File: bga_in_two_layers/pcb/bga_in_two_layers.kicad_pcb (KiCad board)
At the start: 2 copper layers, 25.4 x 35.6 mm, 31 parts, among them CON1 top, CON2 left, CON3 right, CON4 bottom

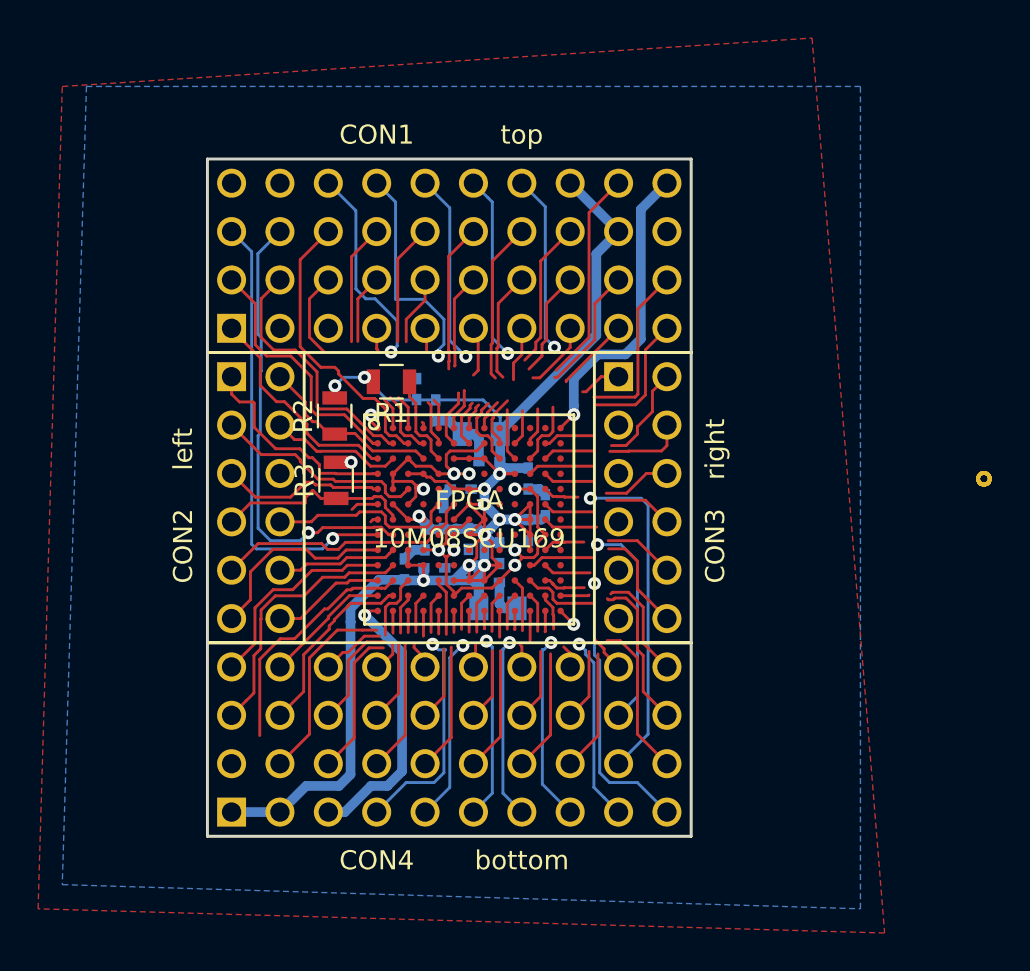
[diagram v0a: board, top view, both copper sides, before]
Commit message: bga_in_two_layers: finished routing, and sent off to oshpark
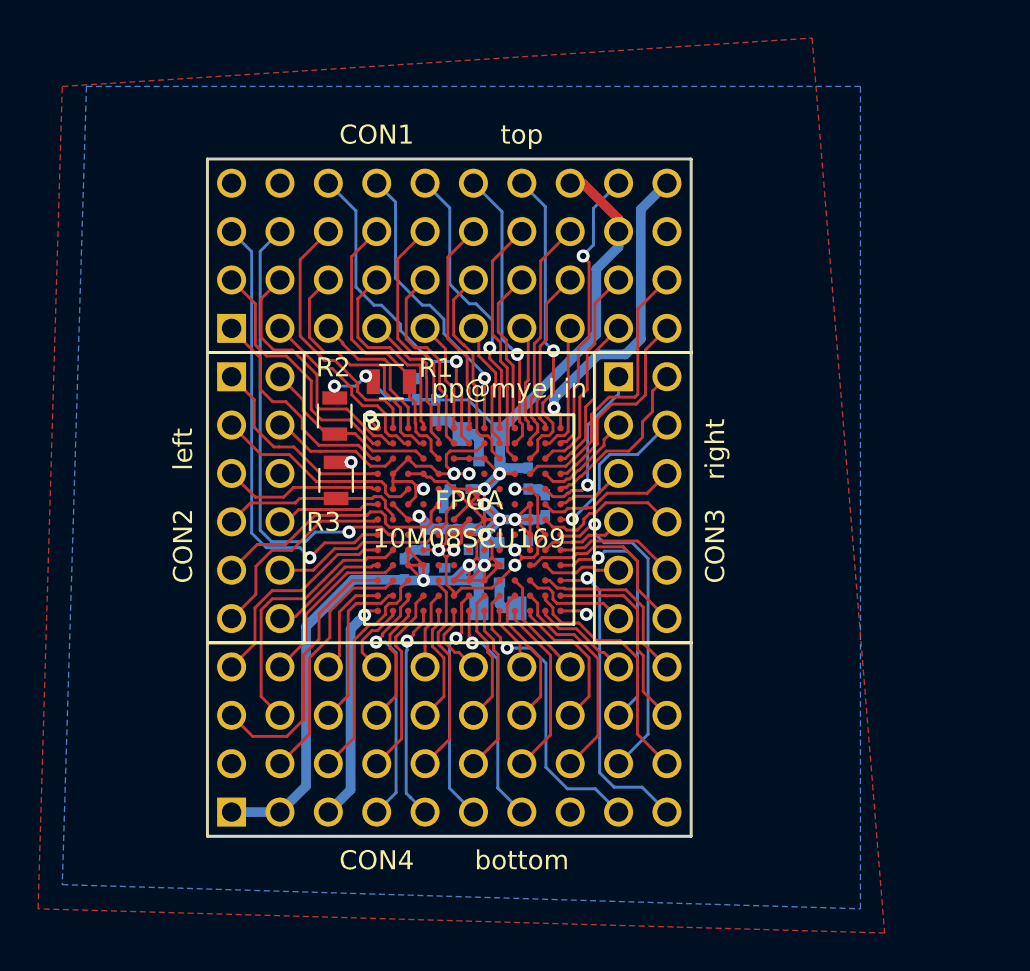
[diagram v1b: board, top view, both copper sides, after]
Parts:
- removed staple_single1, staple_single2, staple_single3, staple_single4, staple_single5, staple_single6, staple_single7: , myelin-kicad:via_single
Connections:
- CON1 pad 10: pin10 -> IO47
- CON1 pad 11: IO46 -> IO0
- CON1 pad 12: pin12 -> IO50
- CON1 pad 13: pin13 -> IO48
- CON1 pad 14: pin14 -> IO2
- CON1 pad 15: pin15 -> fpga_CONF_DONE
- CON1 pad 16: pin16 -> IO6
- CON1 pad 17: pin17 -> IO4
- CON1 pad 18: pin18 -> IO49
- CON1 pad 19: pin19 -> IO3
- CON1 pad 20: pin20 -> IO7
- CON1 pad 21: pin21 -> fpga_DEV_CLRn
- CON1 pad 22: pin22 -> IO70
- CON1 pad 23: pin23 -> IO5
- CON1 pad 24: pin24 -> IO51
- CON1 pad 25: pin25 -> IO9
- CON1 pad 26: pin26 -> IO8
- CON1 pad 27: pin27 -> IO71
- CON1 pad 28: pin28 -> IO85
- CON1 pad 29: pin29 -> IO72
- CON1 pad 30: pin30 -> IO10
- CON1 pad 31: pin31 -> IO52
- CON1 pad 33: pin33 -> IO34
- CON1 pad 34: pin34 -> IO73
- CON1 pad 36: pin36 -> IO33
- CON1 pad 37: pin37 -> IO35
- CON1 pad 38: pin38 -> IO74
- CON1 pad 5: pin5 -> IO46
- CON1 pad 9: pin9 -> IO1
- CON2 pad 10: IO66 -> fpga_TDO
- CON2 pad 11: IO28 -> fpga_TMS
- CON2 pad 12: VREFB2N0 -> IO30
- CON2 pad 8: fpga_TDI -> IO26
- CON2 pad 9: fpga_TDO -> fpga_TDI
- CON3 pad 1: pin1 -> IO76
- CON3 pad 10: pin10 -> IO40
- CON3 pad 11: pin11 -> IO82
- CON3 pad 12: pin12 -> IO80
- CON3 pad 2: pin2 -> CLK3n
- CON3 pad 3: pin3 -> IO75
- CON3 pad 4: pin4 -> IO38
- CON3 pad 5: pin5 -> CLK3p
- CON3 pad 6: pin6 -> IO77
- CON3 pad 7: pin7 -> IO79
- CON3 pad 8: pin8 -> IO78
- CON3 pad 9: pin9 -> IO81
- CON4 pad 10: pin10 -> IO69
- CON4 pad 11: pin11 -> IO53
- CON4 pad 12: pin12 -> IO32
- CON4 pad 13: pin13 -> IO54
- CON4 pad 14: pin14 -> IO55
- CON4 pad 15: pin15 -> DPCLK1
- CON4 pad 16: pin16 -> DPCLK0
- CON4 pad 17: pin17 -> IO13
- CON4 pad 18: pin18 -> IO87
- CON4 pad 19: pin19 -> IO14
- CON4 pad 20: pin20 -> IO56
- CON4 pad 21: pin21 -> IO57
- CON4 pad 22: pin22 -> IO17
- CON4 pad 23: pin23 -> IO58
- CON4 pad 24: pin24 -> IO15
- CON4 pad 25: pin25 -> IO16
- CON4 pad 26: pin26 -> IO19
- CON4 pad 27: pin27 -> IO60
- CON4 pad 28: pin28 -> IO18
- CON4 pad 3: IO67 -> VREFB2N0
- CON4 pad 30: pin30 -> IO61
- CON4 pad 31: pin31 -> IO20
- CON4 pad 32: pin32 -> IO84
- CON4 pad 33: pin33 -> IO59
- CON4 pad 34: pin34 -> IO39
- CON4 pad 35: pin35 -> IO42
- CON4 pad 36: pin36 -> IO21
- CON4 pad 37: pin37 -> IO43
- CON4 pad 38: pin38 -> IO62
- CON4 pad 39: pin39 -> IO44
- CON4 pad 4: IO30 -> IO28
- CON4 pad 40: pin40 -> IO83
- CON4 pad 6: IO69 -> IO68
- CON4 pad 7: IO53 -> IO66
- CON4 pad 8: IO32 -> IO67
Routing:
- net pin34: track 24.0 -> 0.00 mm, vias 1 -> 0
- net pin37: track 21.3 -> 0.00 mm, vias 1 -> 0
- net 3V3: track 110.3 -> 131.1 mm
- net pin12: track 19.6 -> 0.00 mm, vias 1 -> 0
- net IO39: track 0.00 -> 17.3 mm, vias 0 -> 1
- net pin38: track 17.2 -> 0.00 mm
- net IO43: track 0.00 -> 16.3 mm, vias 0 -> 1
- net pin10: track 16.0 -> 0.00 mm
- net IO33: track 0.00 -> 15.3 mm, vias 0 -> 1
- net IO50: track 2.51 -> 17.7 mm, vias 0 -> 1
- net IO7: track 0.00 -> 14.9 mm, vias 0 -> 1
- net IO59: track 2.04 -> 16.0 mm, vias 0 -> 1
- net IO6: track 1.63 -> 15.4 mm, vias 0 -> 1
- net pin33: track 13.6 -> 0.00 mm, vias 1 -> 0
- net pin16: track 13.2 -> 0.00 mm, vias 1 -> 0
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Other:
- board text added: "myelin.nz/ acorn/bgain2"
- board text added: "pp@myel.in"

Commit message: Renumbered IO* pins to match connector pinout
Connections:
- net CLK3n renamed C3_2_CLK3n
- net CLK3p renamed C3_3_CLK3p
- net DPCLK0 renamed C4_16_DPCLK0
- net DPCLK1 renamed C4_15_DPCLK1
- net IO0 renamed C1_11
- net IO1 renamed C1_9
- net IO10 renamed C1_30
- net IO13 renamed C4_17
- net IO14 renamed C4_19
- net IO15 renamed C4_24
- net IO16 renamed C4_25
- net IO17 renamed C4_22
- net IO18 renamed C4_28
- net IO19 renamed C4_26
- net IO2 renamed C1_14
- net IO20 renamed C4_31
- net IO21 renamed C4_36
- net IO22 renamed C1_2
- net IO23 renamed C1_1
- net IO24 renamed C2_1
- net IO25 renamed C2_5
- net IO26 renamed C2_8
- net IO27 renamed C1_3
- net IO28 renamed C4_4
- net IO3 renamed C1_19
- net IO30 renamed C2_12
- net IO32 renamed C4_12
- net IO33 renamed C1_36
- net IO34 renamed C1_33
- net IO35 renamed C1_37
- net IO38 renamed C3_4
- net IO39 renamed C4_34
- net IO4 renamed C1_17
- net IO40 renamed C3_10
- net IO42 renamed C4_35
- net IO43 renamed C4_37
- net IO44 renamed C4_39
- net IO45 renamed C1_6
- net IO46 renamed C1_5
- net IO47 renamed C1_10
- net IO48 renamed C1_13
- net IO49 renamed C1_18
- net IO5 renamed C1_23
- net IO50 renamed C1_12
- net IO51 renamed C1_24
- net IO52 renamed C1_31
- net IO53 renamed C4_11
- net IO54 renamed C4_13
- net IO55 renamed C4_14
- net IO56 renamed C4_20
- net IO57 renamed C4_21
- net IO58 renamed C4_23
- net IO59 renamed C4_33
- net IO6 renamed C1_16
- net IO60 renamed C4_27
- net IO61 renamed C4_30
- net IO62 renamed C4_38
- net IO63 renamed C2_4
- net IO65 renamed C1_7
- net IO66 renamed C4_7
- net IO67 renamed C4_8
- net IO68 renamed C4_6
- net IO69 renamed C4_10
- net IO7 renamed C1_20
- net IO70 renamed C1_22
- net IO71 renamed C1_27
- net IO72 renamed C1_29
- net IO73 renamed C1_34
- net IO74 renamed C1_38
- net IO75 renamed C3_3
- net IO76 renamed C3_1
- net IO77 renamed C3_6
- net IO78 renamed C3_8
- net IO79 renamed C3_7
- net IO8 renamed C1_26
- net IO80 renamed C3_12
- net IO81 renamed C3_9
- net IO82 renamed C3_11
- net IO83 renamed C4_40
- net IO84 renamed C4_32
- net IO85 renamed C1_28
- net IO86 renamed C2_3
- net IO87 renamed C4_18
- net IO9 renamed C1_25
- net VREFB2N0 renamed C4_3_VREFB2N0

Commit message: bga_in_two_layers bringup
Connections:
- net C3_3_CLK3p renamed C3_5_CLK3p
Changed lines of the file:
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@@
   (net 99 C1_9)
   (net 100 C3_2_CLK3n)
-  (net 101 C3_3_CLK3p)
-  (net 102 C4_3_VREFB2N0)
-  (net 103 C4_15_DPCLK1)
-  (net 104 C4_16_DPCLK0)
+  (net 101 C4_3_VREFB2N0)
+  (net 102 C4_15_DPCLK1)
+  (net 103 C4_16_DPCLK0)
+  (net 104 C3_5_CLK3p)
   (net_class Default "This is the default net class."
     (clearance 0.1524)
@@
     (add_net C3_2_CLK3n)
     (add_net C3_3)
-    (add_net C3_3_CLK3p)
     (add_net C3_4)
+    (add_net C3_5_CLK3p)
     (add_net C3_6)
     (add_net C3_7)
@@
       (net 60 C3_6))
     (pad F13 smd circle (at 4.8 -0.8) (size 0.342 0.342) (layers F.Cu F.Paste F.Mask)
-      (net 101 C3_3_CLK3p))
+      (net 104 C3_5_CLK3p))
     (pad G1 smd circle (at -4.8 0) (size 0.342 0.342) (layers F.Cu F.Paste F.Mask)
       (net 9 fpga_TMS))
@@
       (net 93 C4_35))
     (pad L1 smd circle (at -4.8 3.2) (size 0.342 0.342) (layers F.Cu F.Paste F.Mask)
-      (net 102 C4_3_VREFB2N0))
+      (net 101 C4_3_VREFB2N0))
     (pad L2 smd circle (at -4 3.2) (size 0.342 0.342) (layers F.Cu F.Paste F.Mask)
       (net 68 C4_6))
@@
       (net 1 GND))
     (pad N2 smd circle (at -4 4.8) (size 0.342 0.342) (layers F.Cu F.Paste F.Mask)
-      (net 104 C4_16_DPCLK0))
+      (net 103 C4_16_DPCLK0))
     (pad N3 smd circle (at -3.2 4.8) (size 0.342 0.342) (layers F.Cu F.Paste F.Mask)
-      (net 103 C4_15_DPCLK1))
+      (net 102 C4_15_DPCLK1))
     (pad N4 smd circle (at -2.4 4.8) (size 0.342 0.342) (layers F.Cu F.Paste F.Mask)
       (net 76 C4_17))
@@
       (net 59 C3_4))
     (pad 5 thru_hole circle (at -1.27 1.27 270) (size 1.524 1.524) (drill 1.016) (layers *.Cu *.Mask)
-      (net 101 C3_3_CLK3p))
+      (net 104 C3_5_CLK3p))
     (pad 6 thru_hole circle (at -1.27 -1.27 270) (size 1.524 1.524) (drill 1.016) (layers *.Cu *.Mask)
       (net 60 C3_6))
@@
       (net 1 GND))
     (pad 3 thru_hole circle (at -11.43 -1.27) (size 1.524 1.524) (drill 1.016) (layers *.Cu *.Mask)
-      (net 102 C4_3_VREFB2N0))
+      (net 101 C4_3_VREFB2N0))
     (pad 4 thru_hole circle (at -11.43 -3.81) (size 1.524 1.524) (drill 1.016) (layers *.Cu *.Mask)
       (net 67 C4_4))
@@
       (net 75 C4_14))
     (pad 15 thru_hole circle (at -3.81 -1.27) (size 1.524 1.524) (drill 1.016) (layers *.Cu *.Mask)
-      (net 103 C4_15_DPCLK1))
+      (net 102 C4_15_DPCLK1))
     (pad 16 thru_hole circle (at -3.81 -3.81) (size 1.524 1.524) (drill 1.016) (layers *.Cu *.Mask)
-      (net 104 C4_16_DPCLK0))
+      (net 103 C4_16_DPCLK0))
     (pad 17 thru_hole circle (at -1.27 3.81) (size 1.524 1.524) (drill 1.016) (layers *.Cu *.Mask)
       (net 76 C4_17))
@@
   (segment (start 153.761479 56.47259) (end 154.202312 56.031758) (width 0.1524) (layer F.Cu) (net 100))
   (segment (start 157.988001 52.635909) (end 157.988001 51.561999) (width 0.1524) (layer F.Cu) (net 100))
-  (segment (start 153.164872 57.49848) (end 153.241187 57.422165) (width 0.1524) (layer F.Cu) (net 101))
-  (segment (start 153.241187 57.422165) (end 153.441013 57.422165) (width 0.1524) (layer F.Cu) (net 101))
-  (segment (start 153.650663 57.212515) (end 153.650664 57.212514) (width 0.1524) (layer F.Cu) (net 101))
-  (segment (start 153.865753 57.08221) (end 155.00779 57.08221) (width 0.1524) (layer F.Cu) (net 101))
-  (segment (start 155.00779 57.08221) (end 155.448001 56.641999) (width 0.1524) (layer F.Cu) (net 101))
-  (segment (start 155.448001 56.641999) (end 156.21 55.88) (width 0.1524) (layer F.Cu) (net 101))
-  (segment (start 153.735449 57.212514) (end 153.865753 57.08221) (width 0.1524) (layer F.Cu) (net 101))
-  (segment (start 153.441013 57.422165) (end 153.650663 57.212515) (width 0.1524) (layer F.Cu) (net 101))
-  (segment (start 153.650664 57.212514) (end 153.735449 57.212514) (width 0.1524) (layer F.Cu) (net 101))
-  (segment (start 153.650664 57.212514) (end 153.69267 57.212514) (width 0.1524) (layer F.Cu) (net 101))
-  (segment (start 143.564872 61.49848) (end 142.241074 61.49848) (width 0.1524) (layer F.Cu) (net 102))
-  (segment (start 142.241074 61.49848) (end 140.47978 63.259774) (width 0.1524) (layer F.Cu) (net 102))
-  (segment (start 140.47978 63.259774) (end 140.47978 64.590458) (width 0.1524) (layer F.Cu) (net 102))
-  (segment (start 140.47978 64.590458) (end 139.674588 65.39565) (width 0.1524) (layer F.Cu) (net 102))
-  (segment (start 139.674588 68.801502) (end 138.79119 69.6849) (width 0.1524) (layer F.Cu) (net 102))
-  (segment (start 139.674588 65.39565) (end 139.674588 68.801502) (width 0.1524) (layer F.Cu) (net 102))
-  (segment (start 138.79119 69.6849) (end 136.9949 69.6849) (width 0.1524) (layer F.Cu) (net 102))
-  (segment (start 136.9949 69.6849) (end 135.89 68.58) (width 0.1524) (layer F.Cu) (net 102))
-  (segment (start 144.208488 65.058817) (end 144.513287 65.363616) (width 0.1524) (layer F.Cu) (net 103))
-  (segment (start 144.208488 64.339475) (end 144.208488 65.058817) (width 0.1524) (layer F.Cu) (net 103))
-  (segment (start 144.513287 67.576713) (end 144.271999 67.818001) (width 0.1524) (layer F.Cu) (net 103))
-  (segment (start 144.271999 67.818001) (end 143.51 68.58) (width 0.1524) (layer F.Cu) (net 103))
-  (segment (start 144.513287 65.363616) (end 144.513287 67.576713) (width 0.1524) (layer F.Cu) (net 103))
-  (segment (start 145.164872 63.09848) (end 145.164872 63.383091) (width 0.1524) (layer F.Cu) (net 103))
-  (segment (start 145.164872 63.383091) (end 144.208488 64.339475) (width 0.1524) (layer F.Cu) (net 103))
-  (segment (start 144.364872 63.320957) (end 144.364872 63.09848) (width 0.1524) (layer F.Cu) (net 104))
-  (segment (start 143.51 66.04) (end 142.748001 65.278001) (width 0.1524) (layer F.Cu) (net 104))
-  (segment (start 143.255998 64.134998) (end 143.550831 64.134998) (width 0.1524) (layer F.Cu) (net 104))
-  (segment (start 143.550831 64.134998) (end 144.364872 63.320957) (width 0.1524) (layer F.Cu) (net 104))
-  (segment (start 142.748001 65.278001) (end 142.748001 64.642995) (width 0.1524) (layer F.Cu) (net 104))
-  (segment (start 142.748001 64.642995) (end 143.255998 64.134998) (width 0.1524) (layer F.Cu) (net 104))
+  (segment (start 143.564872 61.49848) (end 142.241074 61.49848) (width 0.1524) (layer F.Cu) (net 101))
+  (segment (start 142.241074 61.49848) (end 140.47978 63.259774) (width 0.1524) (layer F.Cu) (net 101))
+  (segment (start 140.47978 63.259774) (end 140.47978 64.590458) (width 0.1524) (layer F.Cu) (net 101))
+  (segment (start 140.47978 64.590458) (end 139.674588 65.39565) (width 0.1524) (layer F.Cu) (net 101))
+  (segment (start 139.674588 68.801502) (end 138.79119 69.6849) (width 0.1524) (layer F.Cu) (net 101))
+  (segment (start 139.674588 65.39565) (end 139.674588 68.801502) (width 0.1524) (layer F.Cu) (net 101))
+  (segment (start 138.79119 69.6849) (end 136.9949 69.6849) (width 0.1524) (layer F.Cu) (net 101))
+  (segment (start 136.9949 69.6849) (end 135.89 68.58) (width 0.1524) (layer F.Cu) (net 101))
+  (segment (start 144.208488 65.058817) (end 144.513287 65.363616) (width 0.1524) (layer F.Cu) (net 102))
+  (segment (start 144.208488 64.339475) (end 144.208488 65.058817) (width 0.1524) (layer F.Cu) (net 102))
+  (segment (start 144.513287 67.576713) (end 144.271999 67.818001) (width 0.1524) (layer F.Cu) (net 102))
+  (segment (start 144.271999 67.818001) (end 143.51 68.58) (width 0.1524) (layer F.Cu) (net 102))
+  (segment (start 144.513287 65.363616) (end 144.513287 67.576713) (width 0.1524) (layer F.Cu) (net 102))
+  (segment (start 145.164872 63.09848) (end 145.164872 63.383091) (width 0.1524) (layer F.Cu) (net 102))
+  (segment (start 145.164872 63.383091) (end 144.208488 64.339475) (width 0.1524) (layer F.Cu) (net 102))
+  (segment (start 144.364872 63.320957) (end 144.364872 63.09848) (width 0.1524) (layer F.Cu) (net 103))
+  (segment (start 143.51 66.04) (end 142.748001 65.278001) (width 0.1524) (layer F.Cu) (net 103))
+  (segment (start 143.255998 64.134998) (end 143.550831 64.134998) (width 0.1524) (layer F.Cu) (net 103))
+  (segment (start 143.550831 64.134998) (end 144.364872 63.320957) (width 0.1524) (layer F.Cu) (net 103))
+  (segment (start 142.748001 65.278001) (end 142.748001 64.642995) (width 0.1524) (layer F.Cu) (net 103))
+  (segment (start 142.748001 64.642995) (end 143.255998 64.134998) (width 0.1524) (layer F.Cu) (net 103))
+  (segment (start 153.164872 57.49848) (end 153.241187 57.422165) (width 0.1524) (layer F.Cu) (net 104))
+  (segment (start 153.241187 57.422165) (end 153.441013 57.422165) (width 0.1524) (layer F.Cu) (net 104))
+  (segment (start 153.650663 57.212515) (end 153.650664 57.212514) (width 0.1524) (layer F.Cu) (net 104))
+  (segment (start 153.865753 57.08221) (end 155.00779 57.08221) (width 0.1524) (layer F.Cu) (net 104))
+  (segment (start 155.00779 57.08221) (end 155.448001 56.641999) (width 0.1524) (layer F.Cu) (net 104))
+  (segment (start 155.448001 56.641999) (end 156.21 55.88) (width 0.1524) (layer F.Cu) (net 104))
+  (segment (start 153.735449 57.212514) (end 153.865753 57.08221) (width 0.1524) (layer F.Cu) (net 104))
+  (segment (start 153.441013 57.422165) (end 153.650663 57.212515) (width 0.1524) (layer F.Cu) (net 104))
+  (segment (start 153.650664 57.212514) (end 153.735449 57.212514) (width 0.1524) (layer F.Cu) (net 104))
+  (segment (start 153.650664 57.212514) (end 153.69267 57.212514) (width 0.1524) (layer F.Cu) (net 104))
   (zone (net 1) (net_name GND) (layer F.Cu) (hatch edge 0.508)
     (connect_pads (clearance 0.254))
